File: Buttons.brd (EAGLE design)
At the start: 85 x 79 mm, 63 parts, among them T1 SI2301, U1 TCA8418RTWR, U2 Tiny85-20-SMT

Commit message: this could be the one neo!
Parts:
- added R3: 1k, SparkFun-Passives:0805
- R1: value 100 -> 1k
- moved CN1 74.6 mm to (5.18, 70.1)
- moved C11 41.4 mm to (47.5, 60.1)
- moved R2 39.4 mm to (40.5, 64.3)
- moved U1 38.6 mm to (12.8, 65.0)
- moved U2 37.7 mm to (42.3, 69.2)
- moved C10 37.5 mm to (45.7, 60.1)
- moved T1 37.3 mm to (44.6, 64.5)
- moved U$1 25.2 mm to (59.0, 56.2)
- moved R1 10.5 mm to (17.8, 57.4), turned to 180 degrees
- turned U$3 to 180 degrees
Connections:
- removed net N$49: U1.8
- removed net N$9: U1.7
- new net N$8: R3.2, U1.1, U1.2, U1.3
- net 3V3@2: now also R3.1
- net N$24: now also U1.4; no longer U1.2
- net N$29: now also U1.5; no longer U1.3
- net N$30: now also U1.6; no longer U1.4
- net N$31: now also U1.7; no longer U1.5
- net N$33: now also U1.8; no longer U1.6
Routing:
- net N$9: track 0.00 -> 164.1 mm
- net N$30: track 118.3 -> 188.1 mm
- net N$29: track 111.9 -> 181.5 mm
- net N$24: track 106.2 -> 175.7 mm
- net N$31: track 125.3 -> 194.3 mm
- net N$33: track 275.9 -> 343.1 mm
- net N$23: track 73.7 -> 140.3 mm
- net N$46: track 76.9 -> 141.9 mm
- net N$45: track 79.2 -> 143.8 mm
- net N$44: track 85.0 -> 149.1 mm
- net N$43: track 87.5 -> 151.0 mm
- net N$42: track 87.4 -> 150.7 mm
- net N$11: track 122.0 -> 59.0 mm, vias 1 -> 2
- net N$41: track 73.7 -> 133.6 mm
- net N$40: track 69.1 -> 122.4 mm
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- added copper zone on layer 16, net N$13
- added copper zone on layer 1, net N$14

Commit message: nailed it!
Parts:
- added INT, RST: TPB2,54, testpad:B2,54
- renumbered CN1 to BAT
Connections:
- new net N$15: INT.TP, U1.24
- new net N$16: RST.TP, U1.20
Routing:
- net N$16: track 0.00 -> 16.4 mm
- net N$15: track 0.00 -> 12.0 mm
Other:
- board text added: "#Pi0CKET"
- board text added: "'"
- board text added: "100k resistor"
- board text added: "100uf cap to Decouple"
- board text added: "10uf cap to Decouple"
- board text added: ";"
- board text added: "<"
- board text added: ">"
- board text added: "?"
- board text added: "Add some battery here!!! Any 3.7v Li-Po should be fine. The bigger the better"
- board text added: "Be careful with the solder. Go slow and steady"
- board text added: "Clicker"
- board text added: "ILI9341 - 2.8" - 18 pin - SPI - no touch SPI screen i hear you cry!! well dont knock it before you try it"
- board text added: "On/Off"
- board text added: "Status"
- board text added: "TP4056 Li-Po Charge/Protect Module for all your battery management needs"
- board text added: "This 10 ohm resistor helps the backlight"
- board text added: "This ATtiny85 acts as a clever switch"
- board text added: "This is the TCA8418 makes life easer when you have all these buttons"
- board text added: "WS2812B neopixel"
- board text added: "a s d f g h j k l"
- board text added: "alt"
- board text added: "bsp"
- board text added: "ctl"
- board text added: "dn"
- board text added: "dont forget the most important part!! The Pi0!! needs SMD header pins, and make sure they are long enough so you can use hats if you want"
- board text added: "ent"
- board text added: "esc"
- board text added: "lft"
- board text added: "q w e r t y u i o p"
- board text added: "rgt"
- board text added: "sft"
- board text added: "sp"
- board text added: "sup"
- board text added: "tab"
- board text added: "this SI2301CDS FET does the heavy switching"
- board text added: "up"
- board text added: "z x c v b n m"

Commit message: final?
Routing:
- net N$33: track 343.1 -> 340.0 mm
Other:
- outline, holes or cut-outs redrawn
- board text added: "Need more info? https://hackaday.io/project/20937-pi0cket-clicker https://twitter.com/Pi0CKET moosepr@gmail.com"
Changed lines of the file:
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@@
 <setting verticaltext="up"/>
 </settings>
-<grid distance="5" unitdist="mil" unit="mil" style="lines" multiple="1" display="yes" altdistance="0.1" altunitdist="mm" altunit="mm"/>
+<grid distance="0.1" unitdist="mm" unit="mm" style="lines" multiple="1" display="yes" altdistance="0.1" altunitdist="mm" altunit="mm"/>
 <layers>
 <layer number="1" name="Top" color="4" fill="1" visible="yes" active="yes"/>
@@
 <layer number="196" name="mValues" color="7" fill="1" visible="no" active="yes"/>
 <layer number="199" name="Displayboard" color="7" fill="1" visible="no" active="yes"/>
-<layer number="200" name="200bmp" color="1" fill="10" visible="yes" active="yes"/>
+<layer number="200" name="200bmp" color="1" fill="10" visible="no" active="yes"/>
 <layer number="201" name="201bmp" color="2" fill="10" visible="no" active="yes"/>
 <layer number="202" name="202bmp" color="3" fill="10" visible="no" active="yes"/>
@@
 <board>
 <plain>
-<wire x1="0" y1="79" x2="85" y2="79" width="0.254" layer="20"/>
-<wire x1="85" y1="0" x2="0" y2="0" width="0.254" layer="20"/>
-<wire x1="0" y1="0" x2="0" y2="79" width="0.254" layer="20"/>
-<wire x1="85" y1="79" x2="85" y2="0" width="0.254" layer="20"/>
+<wire x1="2" y1="79" x2="83" y2="79" width="0.2" layer="20"/>
+<wire x1="83" y1="0" x2="2" y2="0" width="0.2" layer="20"/>
+<wire x1="0" y1="2" x2="0" y2="77" width="0.2" layer="20"/>
 <text x="5.969" y="37.846" size="3.81" layer="21" font="vector" rot="R90">#Pi0CKET</text>
 <text x="78.994" y="64.897" size="3.81" layer="21" font="vector" rot="SR270">#Pi0CKET</text>
 <text x="56.515" y="73.279" size="3.81" layer="22" font="vector" rot="SMR0">#Pi0CKET</text>
 <text x="56.388" y="1.905" size="3.81" layer="22" font="vector" rot="SMR0">#Pi0CKET</text>
-<text x="52.197" y="36.195" size="3.81" layer="22" font="vector" rot="MR0">Clicker</text>
+<text x="50.927" y="30.734" size="3.81" layer="22" font="vector" rot="MR0">Clicker</text>
 <text x="1.27" y="68.961" size="1.4224" layer="21" font="vector">On/Off</text>
 <text x="77.216" y="70.231" size="1.4224" layer="21" font="vector">Status</text>
@@
 SPI screen i hear you cry!!
 well dont knock it before you try it</text>
+<text x="76" y="37.525" size="1.4224" layer="16" rot="MR0">Need more info?
+https://hackaday.io/project/20937-pi0cket-clicker
+https://twitter.com/Pi0CKET
+moosepr@gmail.com</text>
+<wire x1="85" y1="77" x2="85" y2="2" width="0.2" layer="20"/>
+<wire x1="0" y1="2" x2="2" y2="0" width="0.2" layer="20" curve="90"/>
+<wire x1="85" y1="2" x2="83" y2="0" width="0.2" layer="20" curve="-90"/>
+<wire x1="83" y1="79" x2="85" y2="77" width="0.2" layer="20" curve="-90"/>
+<wire x1="0" y1="77" x2="2" y2="79" width="0.2" layer="20" curve="-90"/>
 </plain>
 <attributes>
@@
 <elements>
 <element name="PI1" library="RPI-Zero" package="RASPBERRYPI_BASTELSTUBE_V13_RASPI_BOARD_B+_FULL" value="RPI-ZERO" x="10" y="78.5" rot="MR180"/>
-<element name="R1" library="resistor" package="R0805" value="1k" x="17.8435" y="57.4415" rot="MR180"/>
+<element name="R1" library="resistor" package="R0805" value="1k" x="17.8435" y="57.4415" smashed="yes" rot="MR180">
+<attribute name="NAME" x="17.2085" y="56.1715" size="0.6096" layer="26" rot="MR180"/>
+<attribute name="VALUE" x="17.2085" y="59.9815" size="1.27" layer="28" rot="MR180"/>
+</element>
 <element name="U$2" library="ili9341" package="ILI9341-2.8" value="ILI9341-2.8" x="42.5" y="54"/>
 <element name="U1" library="Texas Instruments_By_element14_Batch_1" package="QFN50P400X400X80-25N" value="TCA8418RTWR" x="12.834315625" y="64.982840625" smashed="yes" rot="MR0">
@@
 <element name="R2" library="SparkFun-Passives" package="0603-RES" value="100K" x="40.5" y="64.3" rot="MR270"/>
 <element name="C10" library="rcl" package="C0603K" value="100nF" x="45.7" y="60.1" smashed="yes" rot="MR90">
-<attribute name="NAME" x="45.207" y="55.998" size="1.016" layer="26" rot="MR90"/>
+<attribute name="NAME" x="45.207" y="55.798" size="1.016" layer="26" rot="MR90"/>
 <attribute name="VALUE" x="43.923" y="55.363" size="1.016" layer="28" rot="MR90"/>
 </element>
@@
 <wire x1="82.6" y1="30.2" x2="82.7" y2="30.2" width="0.1524" layer="1"/>
 <wire x1="82.7" y1="30.2" x2="84.4" y2="28.7" width="0.1524" layer="1"/>
-<wire x1="84.4" y1="28.7" x2="84.4" y2="0.6" width="0.1524" layer="1"/>
-<wire x1="84.4" y1="0.6" x2="0.9" y2="0.6" width="0.1524" layer="1"/>
-<wire x1="0.9" y1="0.6" x2="0.6" y2="0.9" width="0.1524" layer="1"/>
-<wire x1="0.6" y1="0.9" x2="0.6" y2="31.2" width="0.1524" layer="1"/>
-<wire x1="0.6" y1="31.2" x2="1.5" y2="32" width="0.1524" layer="1"/>
+<wire x1="84.4" y1="28.7" x2="84.4" y2="3.4" width="0.1524" layer="1"/>
+<wire x1="0.6" y1="3.4" x2="0.6" y2="3.3" width="0.1524" layer="1"/>
+<wire x1="0.6" y1="31.2" x2="0.6" y2="3.4" width="0.1524" layer="1"/>
+<wire x1="1.5" y1="32" x2="0.6" y2="31.2" width="0.1524" layer="1"/>
 <wire x1="78.5" y1="31.2" x2="80.1" y2="29.6" width="0.1524" layer="1"/>
 <contactref element="U1" pad="8"/>
@@
 <wire x1="37.4" y1="34.4" x2="39.5" y2="36.5" width="0.1524" layer="16"/>
 <wire x1="12.4" y1="34.4" x2="37.4" y2="34.4" width="0.1524" layer="16"/>
+<wire x1="3.3" y1="0.6" x2="0.6" y2="3.3" width="0.1524" layer="1" curve="-90"/>
+<wire x1="84.4" y1="3.4" x2="81.6" y2="0.6" width="0.1524" layer="1" curve="-90"/>
+<wire x1="81.6" y1="0.6" x2="3.3" y2="0.6" width="0.1524" layer="1"/>
 </signal>
 <signal name="N$38">

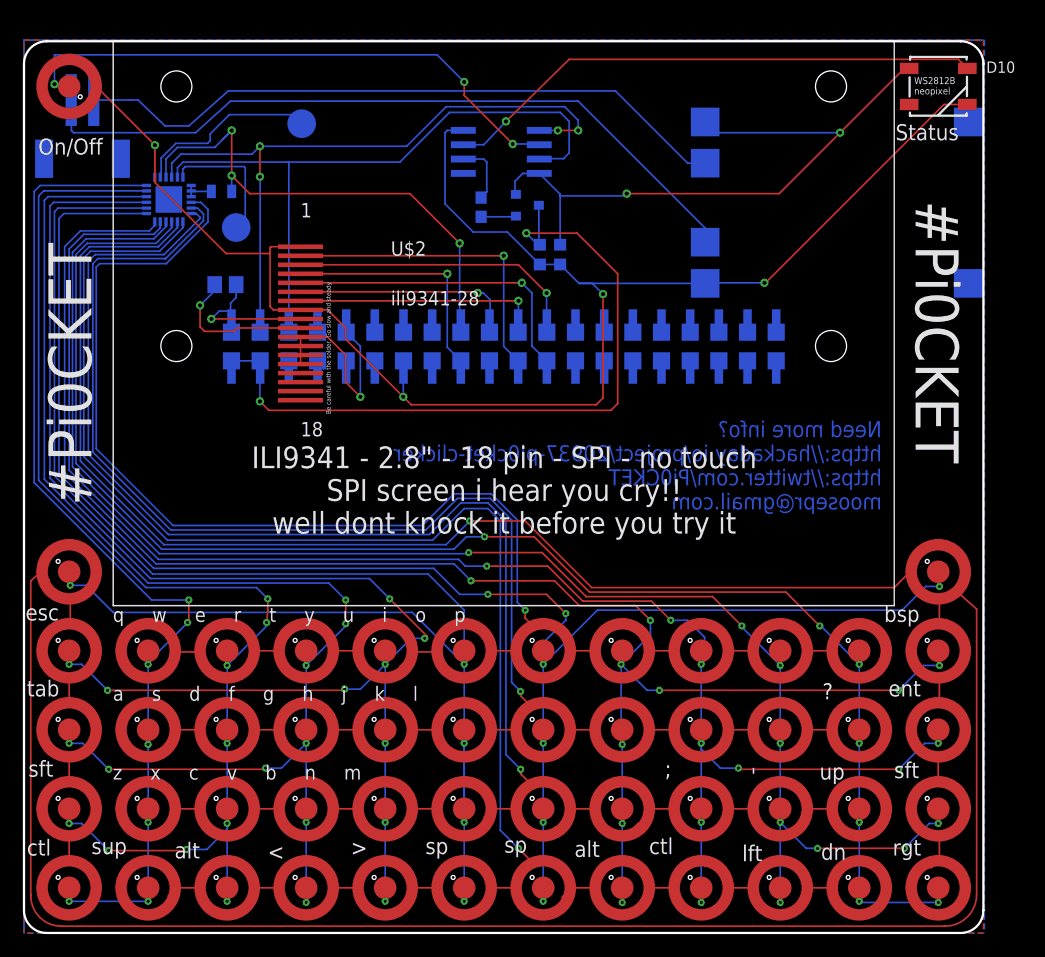
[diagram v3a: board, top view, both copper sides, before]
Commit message: changed the tiny85 to a tiny88, the power button is now a side press jobby, and moved to the back along with the neopixel.
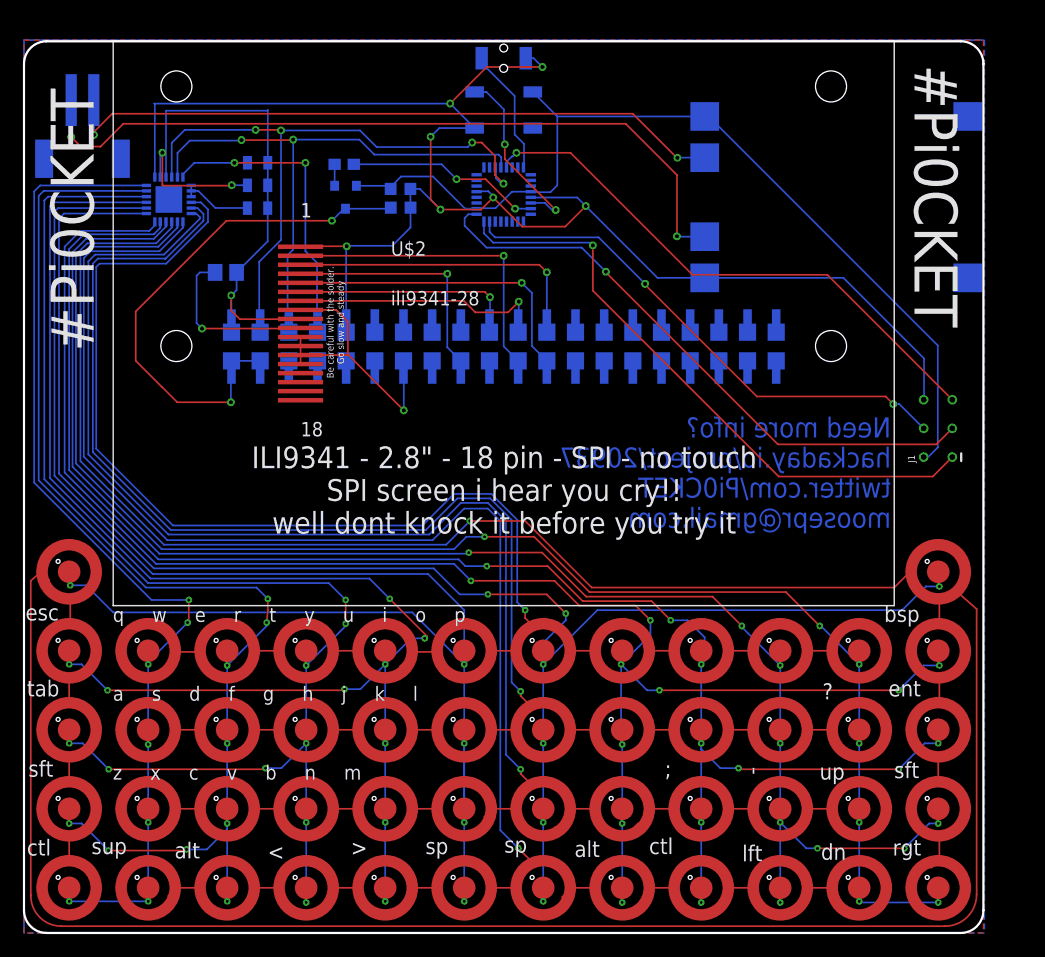
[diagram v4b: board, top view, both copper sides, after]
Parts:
- removed INT, RST: TPB2,54, testpad:B2,54
- removed U$3: 5MMSNAP, 5mmSNAP:5MMSNAP
- removed U2: Tiny85-20-SMT, SparkFun-DigitalIC:SO08-EIAJ
- added J1: AVR_SPI_PROG_3X2TESTPOINTS, SparkFun-Connectors:2X3_TEST_POINTS
- added R4, R5: 1k, SparkFun-Passives:0805
- added S1: MOMENTARY-SWITCH-SPST-SMD-RIGHT-ANGLE, SparkFun-Switches:TACTILE_SWITCH_SMD_RIGHT_ANGLE
- added U3: ATTINY88-MU, attiny88:32M1-A
- moved D10 38.6 mm to (42.5, 72.9), flipped to the bottom
- moved T1 16.1 mm to (28.5, 65.2), turned to 0 degrees
- moved C11 15.3 mm to (33.4, 65.9), turned to 180 degrees
- moved C10 13.0 mm to (33.4, 64.3), turned to 0 degrees
- moved R2 12.7 mm to (28.4, 68.1), turned to 0 degrees
- moved R3 3.52 mm to (20.7, 64.2)
- moved R1 1.08 mm to (17.9, 58.5)
- moved U$1 0.49 mm to (59.0, 56.7)
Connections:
- net 5V0@2 renamed VIN
- net N$1 renamed RST
- net N$2 renamed SCLK
- net N$3 renamed MOSI
- net N$4 renamed MISO
- net N$6 renamed DCX
- net N$7 renamed CS
- removed net 3V3@1: PI1.1, R1.2, U$2.P$9
- removed net 3V3@2: PI1.17, R3.1, U1.21
- removed net GND@1: PI1.9, U$2.P$11, U$2.P$12, U$2.P$13, U$2.P$14
- removed net N$11: C11.1, D10.1, T1.2, U$1.OUT+, U2.8
- removed net N$12: U$3.P$1, U2.6
- removed net N$15: INT.TP, U1.24
- removed net N$18: D10.4, U2.3
- removed net N$28: PI1.3, U1.22, U2.5
- removed net N$34: PI1.5, U1.23, U2.7
- new net 3V3: PI1.1, R1.2, R3.1, R4.2, R5.1, U$2.P$9, U1.21
- new net INT: PI1.7, R4.1, U1.24
- new net ISP-MISO: J1.1, U3.16
- new net ISP-MOSI: J1.4, U3.15
- new net ISP-RST: J1.5, U3.29
- new net ISP-SCK: J1.3, U3.17
- new net N$1: S1.1, U3.32
- new net N$2: D10.4, U3.6
- new net SCL: PI1.5, U1.23, U3.28
- new net SDA: PI1.3, U1.22, U3.27
- new net VCC: C11.1, D10.1, J1.2, T1.2, U$1.OUT+, U3.18, U3.4
- net GND: now also J1.6, PI1.9, S1.2, U$2.P$11, U$2.P$12, U$2.P$13, U$2.P$14, U3.21, U3.5; no longer U$3.P$2, U2.4
- net N$16: now also R5.2; no longer RST.TP
- net N$19: now also U3.7; no longer U2.2
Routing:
- net VCC: track 0.00 -> 82.4 mm
- net N$28: track 60.7 -> 0.00 mm, vias 4 -> 0
- net N$11: track 59.0 -> 0.00 mm, vias 2 -> 0
- net N$34: track 58.7 -> 0.00 mm
- net SDA: track 0.00 -> 56.8 mm, vias 0 -> 4
- net ISP-MISO: track 0.00 -> 54.5 mm, vias 0 -> 1
- net ISP-SCK: track 0.00 -> 53.7 mm, vias 0 -> 1
- net N$12: track 50.9 -> 0.00 mm, vias 3 -> 0
- net SCL: track 0.00 -> 50.2 mm, vias 0 -> 2
- net ISP-RST: track 0.00 -> 49.4 mm, vias 0 -> 1
- net N$18: track 48.1 -> 0.00 mm, vias 1 -> 0
- net ISP-MOSI: track 0.00 -> 46.6 mm, vias 0 -> 2
- net 3V3@2: track 45.1 -> 0.00 mm, vias 3 -> 0
- net 3V3: track 0.00 -> 43.8 mm, vias 0 -> 1
- net INT: track 0.00 -> 28.1 mm, vias 0 -> 2
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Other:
- board text added: "Need more info? hackaday.io/project/20937 twitter.com/Pi0CKET moosepr@gmail.com"
- board text added: "This ATtiny88 acts as a clever switch"
- board text added: "some 10k ressistors to act as pull-up"
- board text removed: "Need more info? https://hackaday.io/project/20937-pi0cket-clicker https://twitter.com/Pi0CKET moosepr@gmail.com"
- board text removed: "On/Off"
- board text removed: "Status"
- board text removed: "This ATtiny85 acts as a clever switch"
- board text removed: "WS2812B neopixel"

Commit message: some polish
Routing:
- net N$16: track 12.7 -> 13.9 mm
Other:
- board text added: "A nice little switch to let you get things going or stopping"
- board text added: "GND"
- board text added: "ISP so you can tweak the tiny to your needs"
- board text added: "MISO"
- board text added: "MOSI"
- board text added: "Neopixel to keep you up to date with the current status"
- board text added: "RST"
- board text added: "SCK"
- board text added: "VCC"

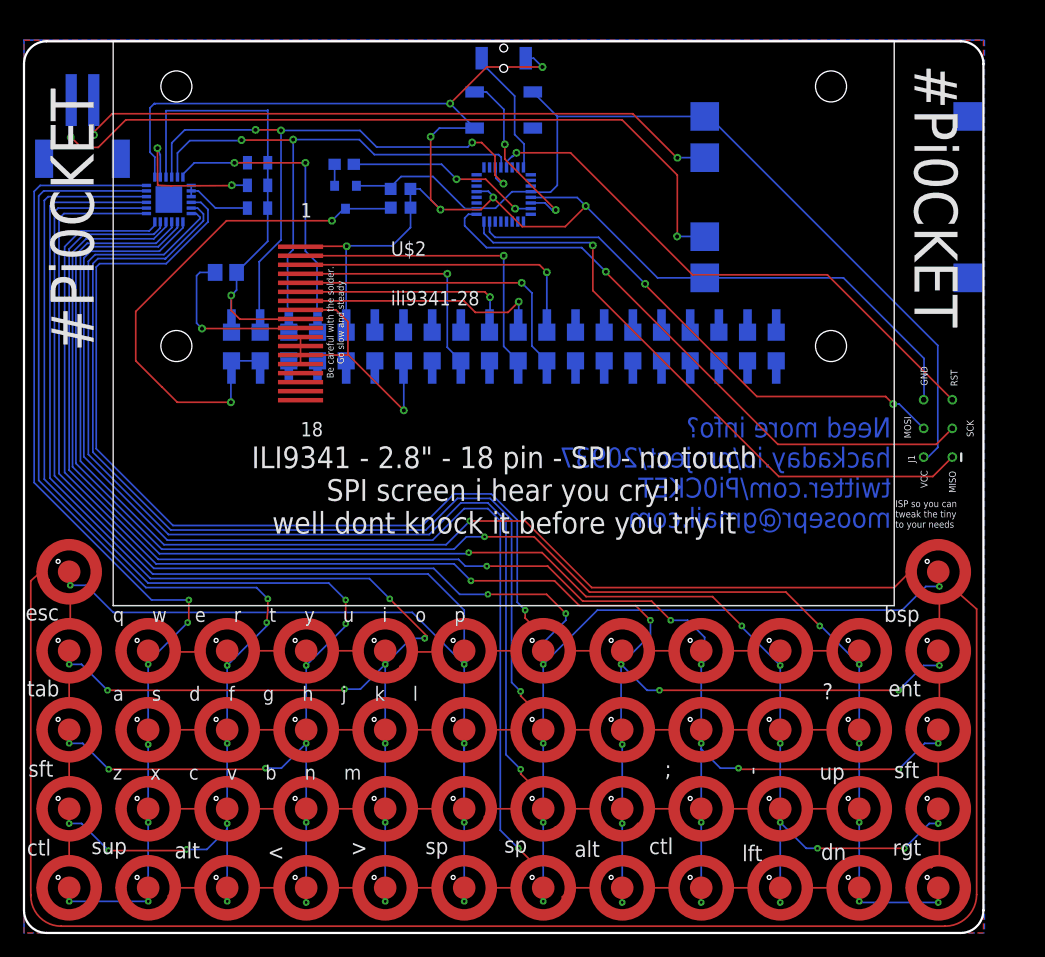
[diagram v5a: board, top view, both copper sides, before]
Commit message: changed to atmega328
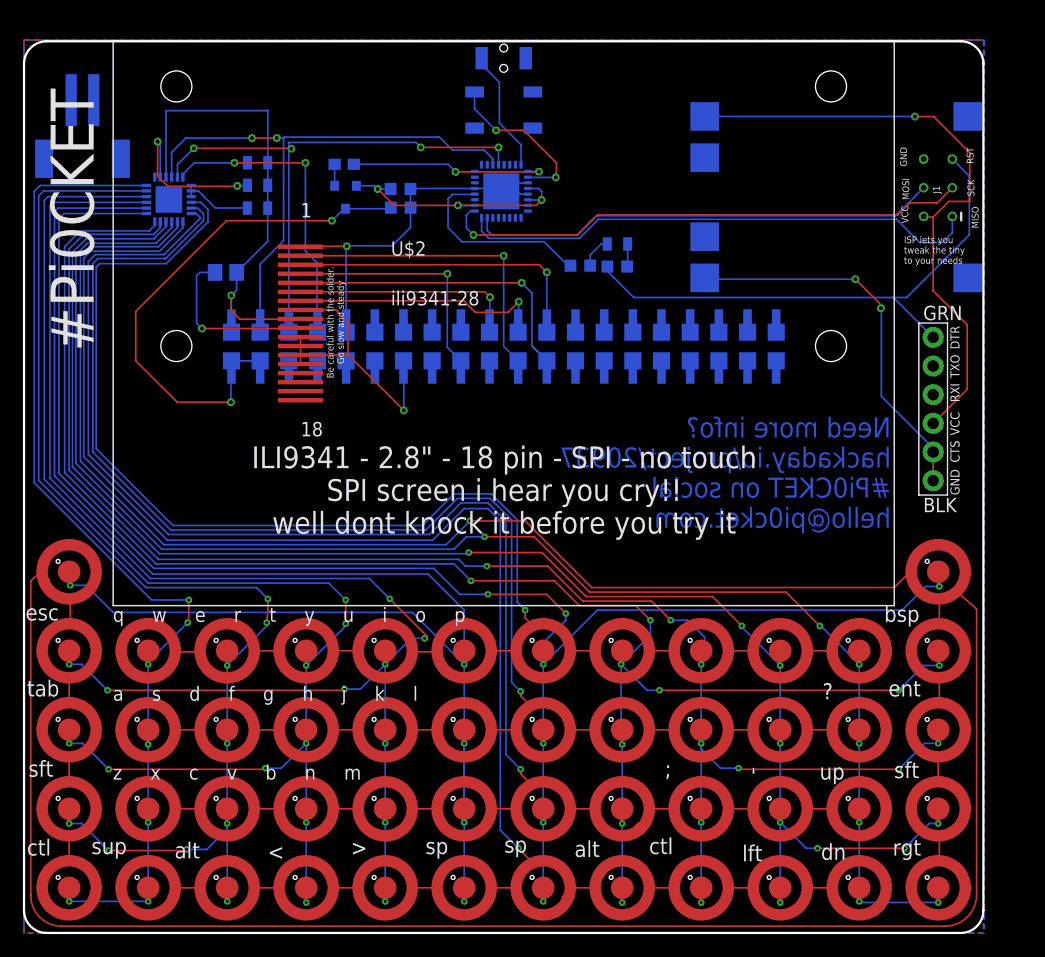
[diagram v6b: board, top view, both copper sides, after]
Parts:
- added C12, C13: 100nF, rcl:C0603K
- added J2: (no value), SparkFun-Connectors:6_PIN_SERIAL_TARGET_SIDE_W_SILK
- added R6: 1k, SparkFun-Passives:0805
- U3: value ATTINY88-MU -> (none); device attiny88:32M1-A -> SparkFun-IC-Microcontroller:MLF32-PAD
- moved J1 21.3 mm to (81.0, 66.0)
- moved U3 0.35 mm to (42.3, 65.7)
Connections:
- removed net N$19: R2.1, U3.7
- removed net N$2: D10.4, U3.6
- new net FET: R2.1, U3.1
- new net N$3: C13.2, U3.20
- new net N$4: C12.1, R6.2, U3.29
- new net NEO: D10.4, U3.2
- new net RX: J2.P$3, U3.30
- new net TX: J2.P$2, U3.31
- net GND: now also J2.P$5, J2.P$6, U3.3, U3.PAD
- net ISP-RST: now also C12.2, J2.P$1; no longer U3.29
- net VCC: now also C13.1, J2.P$4, R6.1, U3.6
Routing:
- net GND: track 170.4 -> 94.5 mm, vias 8 -> 4
- net N$37: track 68.4 -> 0.00 mm, vias 2 -> 0
- net N$36: track 59.8 -> 0.00 mm, vias 2 -> 0
- net FET: track 0.00 -> 17.7 mm, vias 0 -> 2
- net N$3: track 0.00 -> 17.3 mm
- net N$19: track 17.3 -> 0.00 mm, vias 2 -> 0
- net N$2: track 16.5 -> 0.00 mm, vias 2 -> 0
- net NEO: track 0.00 -> 14.5 mm, vias 0 -> 2
- net ISP-MISO: track 54.5 -> 46.5 mm, vias 1 -> 0
- net ISP-SCK: track 53.7 -> 47.1 mm
- net SDA: track 56.8 -> 50.6 mm, vias 4 -> 2
- net ISP-MOSI: track 46.6 -> 41.7 mm, vias 2 -> 0
- net N$4: track 0.00 -> 2.02 mm
- net CS: track 27.4 -> 29.2 mm
- net VCC: track 82.4 -> 80.8 mm, vias 0 -> 4
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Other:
- board text added: "ISP lets you tweak the tiny to your needs"
- board text added: "Need more info? hackaday.io/project/20937 #Pi0CKET on social hello@pi0cket.com"
- board text removed: "ISP so you can tweak the tiny to your needs"
- board text removed: "Need more info? hackaday.io/project/20937 twitter.com/Pi0CKET moosepr@gmail.com"
